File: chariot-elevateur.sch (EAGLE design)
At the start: 0 parts

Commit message: Placement des gros composants
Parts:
- added AX12_AR, AX12_AV: DYNAMIXEL-1X03AX, 1NTech_pinhead:DYNAMIXEL-1X03AX
- added ENCODEUR_DROIT, ENCODEUR_GAUCHE: JST-04GH-V, con-jst:JST-04GH-V
- added JUMPER: JST-03, con-jst:JST-03
- added LED2: green, led:LEDSMT1206
- added LED3: orange, led:LEDSMT1206
- added PAS_A_PAS: (no value), jst-ph:JST-PH6
- added Q1: BSS138, transistor-small-signal:BSS123
- added R2, R3: 10k, resistor:R-EU_R0805
- added R4, R5: 330, resistor:R-EU_R0805
- added S1: A4988-BREAKOUT, stepper:A4988-BREAKOUT
- added S3: TL36PO, switch:TL36PO
- added U$1: TEENSY_3.5_DIL+USB, Teensy_libSG:TEENSY_3.5_DIL+USB
- added U1: WIZ820IO, wiznet:WIZ820IO
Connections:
- new net +3V3: Q1.G, R2.1, R5.1, S3.S
- new net +5V: R3.1
- new net CHOOSE_COLOR: LED3.C, R4.2, S3.P
- new net GND: LED2.C, S3.O
- new net N$7: LED2.A, R4.1
- new net N$8: LED3.A, R5.2
- new net SERIAL_AX12: Q1.S, R2.2
- new net SERIAL_AX12_5V: Q1.D, R3.2

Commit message: more components
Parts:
- added ENDSTOP: JST-03, con-jst:JST-03
- added FUMIGENE: DYNAMIXEL-1X03XL, 1NTech_pinhead:DYNAMIXEL-1X03XL
- added PHARES_AR, PHARES_AV: JST-05, con-jst:JST-05
- added RASPBERRY: JST-06, con-jst:JST-06
- added TOF_AR: JST-08, con-jst:JST-08
- added VESC: (no value), pinhead:PINHD-1X3
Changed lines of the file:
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@@
 <part name="R3" library="resistor" library_urn="urn:adsk.eagle:library:348" deviceset="R-EU_" device="R0805" package3d_urn="urn:adsk.eagle:package:26059/1" value="10k"/>
 <part name="SUPPLY26" library="supply2" library_urn="urn:adsk.eagle:library:372" deviceset="+5V" device=""/>
+<part name="VESC" library="pinhead" library_urn="urn:adsk.eagle:library:325" deviceset="PINHD-1X3" device="" package3d_urn="urn:adsk.eagle:package:22458/2"/>
+<part name="TOF_AR" library="con-jst" deviceset="JST-08" device=""/>
+<part name="PHARES_AR" library="con-jst" deviceset="JST-05" device=""/>
+<part name="PHARES_AV" library="con-jst" deviceset="JST-05" device=""/>
+<part name="FUMIGENE" library="1NTech_pinhead" deviceset="DYNAMIXEL-1X03" device="XL"/>
+<part name="ENDSTOP" library="con-jst" deviceset="JST-03" device=""/>
+<part name="RASPBERRY" library="con-jst" deviceset="JST-06" device=""/>
 </parts>
 <sheets>
@@
 <attribute name="VALUE" x="48.895" y="86.995" size="1.778" layer="96"/>
 </instance>
+<instance part="VESC" gate="A" x="35.56" y="116.84" smashed="yes">
+<attribute name="NAME" x="29.21" y="122.555" size="1.778" layer="95"/>
+<attribute name="VALUE" x="29.21" y="109.22" size="1.778" layer="96"/>
+</instance>
+<instance part="TOF_AR" gate="G$1" x="66.04" y="121.92" smashed="yes">
+<attribute name="NAME" x="62.992" y="124.714" size="1.778" layer="95"/>
+</instance>
+<instance part="PHARES_AR" gate="G$1" x="88.9" y="114.3" smashed="yes">
+<attribute name="NAME" x="85.852" y="117.094" size="1.778" layer="95"/>
+</instance>
+<instance part="PHARES_AV" gate="G$1" x="106.68" y="114.3" smashed="yes">
+<attribute name="NAME" x="103.632" y="117.094" size="1.778" layer="95"/>
+</instance>
+<instance part="FUMIGENE" gate="G$1" x="127" y="109.22" smashed="yes" rot="R90"/>
+<instance part="ENDSTOP" gate="G$1" x="33.02" y="106.68" smashed="yes">
+<attribute name="NAME" x="29.972" y="109.474" size="1.778" layer="95"/>
+</instance>
+<instance part="RASPBERRY" gate="G$1" x="88.9" y="93.98" smashed="yes">
+<attribute name="NAME" x="85.852" y="96.774" size="1.778" layer="95"/>
+</instance>
 </instances>

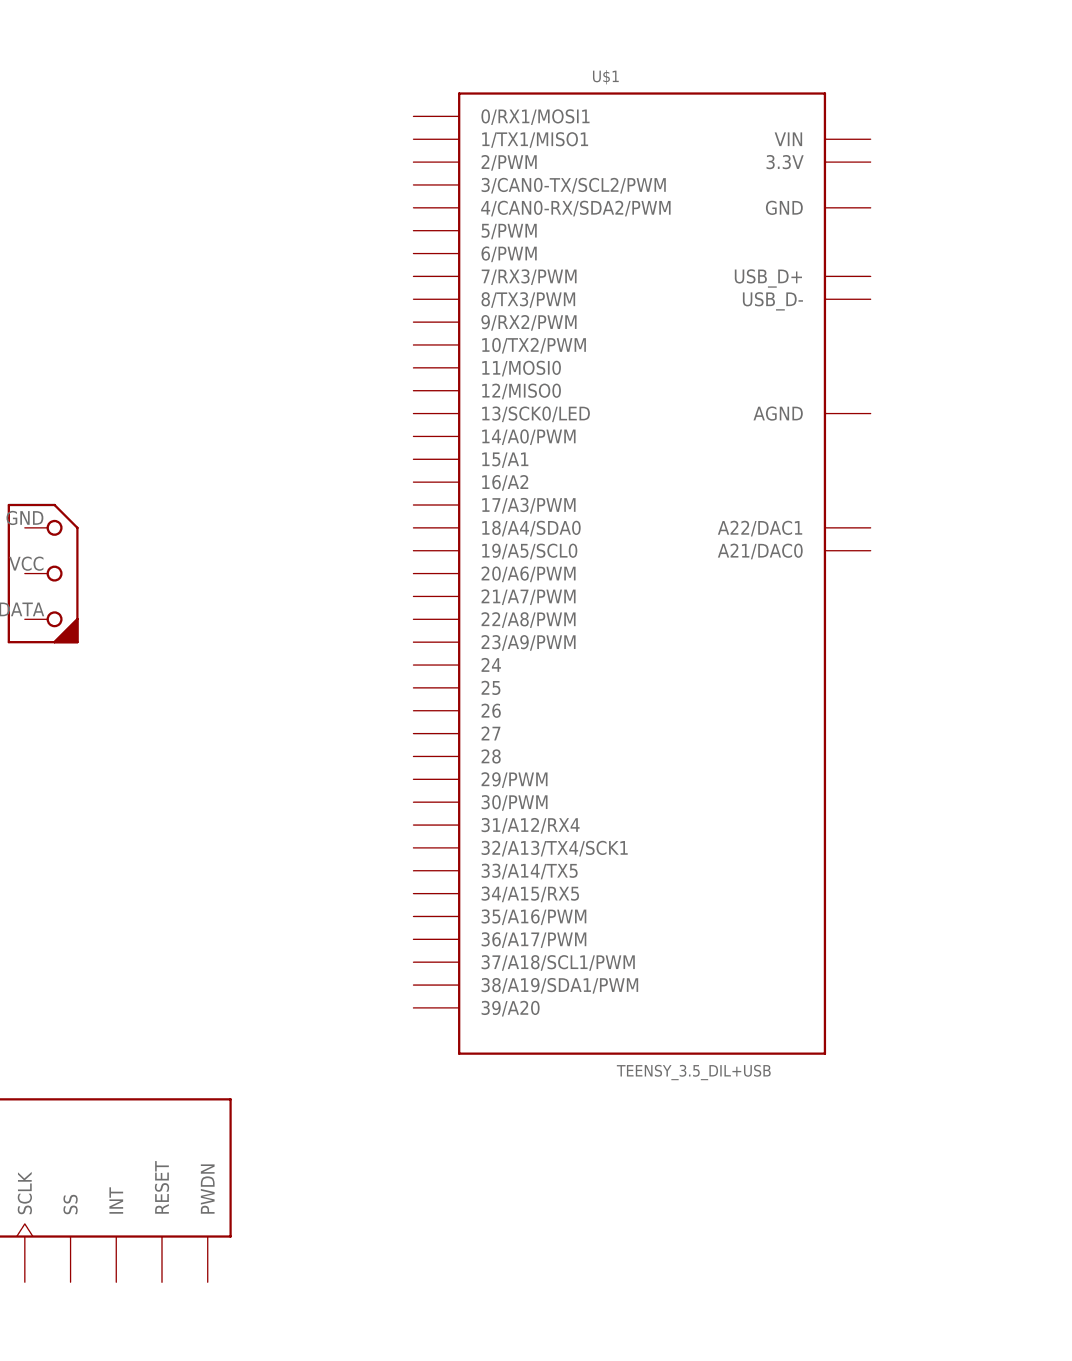
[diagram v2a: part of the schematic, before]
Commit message: Add power connector
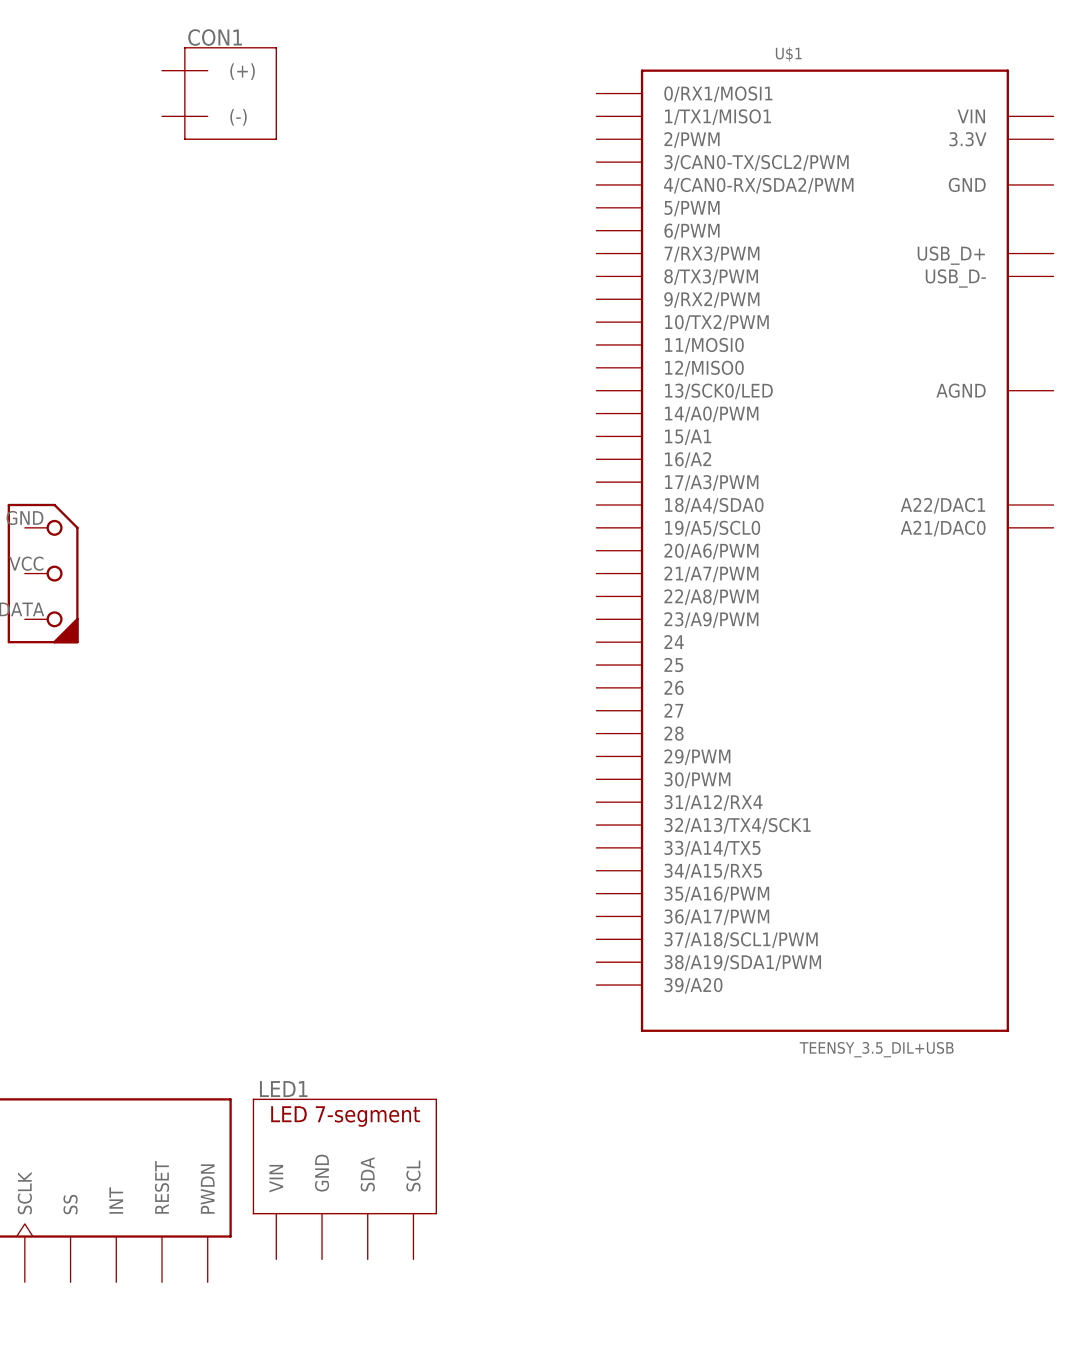
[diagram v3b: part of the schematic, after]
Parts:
- added CON1: XT-60, con-xt:XT-60
- added LED1: ADAFRUIT_7-SEGMENT-LED, Adafruit-7-segment:ADAFRUIT_7-SEGMENT-LED
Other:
- moved on the sheet: U$1
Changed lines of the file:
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@@
 <part name="ENDSTOP" library="con-jst" deviceset="JST-03" device=""/>
 <part name="RASPBERRY" library="con-jst" deviceset="JST-06" device=""/>
+<part name="LED1" library="Adafruit-7-segment" deviceset="ADAFRUIT_7-SEGMENT-LED" device=""/>
+<part name="CON1" library="con-xt" deviceset="XT-60" device=""/>
 </parts>
 <sheets>
@@
 <attribute name="SHEET" x="230.505" y="5.08" size="2.54" layer="94"/>
 </instance>
-<instance part="U$1" gate="G$1" x="195.58" y="109.22" smashed="yes">
-<attribute name="NAME" x="189.992" y="163.83" size="1.27" layer="95" font="vector" ratio="15"/>
-<attribute name="VALUE" x="192.786" y="53.34" size="1.27" layer="96" font="vector" ratio="15"/>
+<instance part="U$1" gate="G$1" x="215.9" y="111.76" smashed="yes">
+<attribute name="NAME" x="210.312" y="166.37" size="1.27" layer="95" font="vector" ratio="15"/>
+<attribute name="VALUE" x="213.106" y="55.88" size="1.27" layer="96" font="vector" ratio="15"/>
 </instance>
 <instance part="U1" gate="G$1" x="127" y="35.56" smashed="yes"/>
@@
 <attribute name="NAME" x="85.852" y="96.774" size="1.778" layer="95"/>
 </instance>
+<instance part="LED1" gate="G$1" x="162.56" y="38.1" smashed="yes">
+<attribute name="NAME" x="152.908" y="51.054" size="1.778" layer="95"/>
+</instance>
+<instance part="CON1" gate="G$1" x="147.32" y="162.56" smashed="yes">
+<attribute name="NAME" x="145.034" y="167.894" size="1.778" layer="95"/>
+</instance>
 </instances>

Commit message: placement connecteurs
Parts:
- VESC: device pinhead:PINHD-1X3 -> pinhead:PINHD-1X3/90
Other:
- moved on the sheet: CON1
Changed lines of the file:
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@@
 <part name="PAS_A_PAS" library="jst-ph" deviceset="JST-PH6" device=""/>
 <part name="S1" library="stepper" deviceset="A4988-BREAKOUT" device=""/>
-<part name="S3" library="switch" library_urn="urn:adsk.eagle:library:380" deviceset="TL36PO" device="" package3d_urn="urn:adsk.eagle:package:27745/1">
+<part name="S3" library="switch" deviceset="TL36PO" device="" package3d_urn="urn:adsk.eagle:package:27745/1">
 <attribute name="RS" value="913-9069"/>
 </part>
-<part name="LED2" library="led" library_urn="urn:adsk.eagle:library:259" deviceset="LED" device="SMT1206" package3d_urn="urn:adsk.eagle:package:15796/1" value="green"/>
-<part name="LED3" library="led" library_urn="urn:adsk.eagle:library:259" deviceset="LED" device="SMT1206" package3d_urn="urn:adsk.eagle:package:15796/1" value="orange"/>
+<part name="LED2" library="led" library_urn="urn:adsk.eagle:library:259" deviceset="LED" device="SMT1206" package3d_urn="urn:adsk.eagle:package:15796/2" value="green"/>
+<part name="LED3" library="led" library_urn="urn:adsk.eagle:library:259" deviceset="LED" device="SMT1206" package3d_urn="urn:adsk.eagle:package:15796/2" value="orange"/>
 <part name="SUPPLY27" library="supply2" library_urn="urn:adsk.eagle:library:372" deviceset="GND" device=""/>
-<part name="R4" library="resistor" library_urn="urn:adsk.eagle:library:348" deviceset="R-EU_" device="R0805" package3d_urn="urn:adsk.eagle:package:26059/1" value="330"/>
-<part name="R5" library="resistor" library_urn="urn:adsk.eagle:library:348" deviceset="R-EU_" device="R0805" package3d_urn="urn:adsk.eagle:package:26059/1" value="330"/>
-<part name="Q1" library="transistor-small-signal" library_urn="urn:adsk.eagle:library:401" deviceset="BSS123" device="" package3d_urn="urn:adsk.eagle:package:29752/1" value="BSS138"/>
-<part name="R2" library="resistor" library_urn="urn:adsk.eagle:library:348" deviceset="R-EU_" device="R0805" package3d_urn="urn:adsk.eagle:package:26059/1" value="10k"/>
-<part name="R3" library="resistor" library_urn="urn:adsk.eagle:library:348" deviceset="R-EU_" device="R0805" package3d_urn="urn:adsk.eagle:package:26059/1" value="10k"/>
+<part name="R4" library="resistor" library_urn="urn:adsk.eagle:library:348" deviceset="R-EU_" device="R0805" package3d_urn="urn:adsk.eagle:package:23553/2" value="330"/>
+<part name="R5" library="resistor" library_urn="urn:adsk.eagle:library:348" deviceset="R-EU_" device="R0805" package3d_urn="urn:adsk.eagle:package:23553/2" value="330"/>
+<part name="Q1" library="transistor-small-signal" library_urn="urn:adsk.eagle:library:401" deviceset="BSS123" device="" package3d_urn="urn:adsk.eagle:package:28738/2" value="BSS138"/>
+<part name="R2" library="resistor" library_urn="urn:adsk.eagle:library:348" deviceset="R-EU_" device="R0805" package3d_urn="urn:adsk.eagle:package:23553/2" value="10k"/>
+<part name="R3" library="resistor" library_urn="urn:adsk.eagle:library:348" deviceset="R-EU_" device="R0805" package3d_urn="urn:adsk.eagle:package:23553/2" value="10k"/>
 <part name="SUPPLY26" library="supply2" library_urn="urn:adsk.eagle:library:372" deviceset="+5V" device=""/>
-<part name="VESC" library="pinhead" library_urn="urn:adsk.eagle:library:325" deviceset="PINHD-1X3" device="" package3d_urn="urn:adsk.eagle:package:22458/2"/>
+<part name="VESC" library="pinhead" library_urn="urn:adsk.eagle:library:325" deviceset="PINHD-1X3" device="/90" package3d_urn="urn:adsk.eagle:package:22459/2"/>
 <part name="TOF_AR" library="con-jst" deviceset="JST-08" device=""/>
 <part name="PHARES_AR" library="con-jst" deviceset="JST-05" device=""/>
@@
 <attribute name="NAME" x="152.908" y="51.054" size="1.778" layer="95"/>
 </instance>
-<instance part="CON1" gate="G$1" x="147.32" y="162.56" smashed="yes">
-<attribute name="NAME" x="145.034" y="167.894" size="1.778" layer="95"/>
+<instance part="CON1" gate="G$1" x="144.78" y="160.02" smashed="yes">
+<attribute name="NAME" x="142.494" y="165.354" size="1.778" layer="95"/>
 </instance>
 </instances>

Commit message: end-of-the-day commit
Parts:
- removed RASPBERRY: JST-06, con-jst:JST-06
- added C1, C2, C3, C4: 22µF, resistor:C-EUC0805
- added C5, C6: 1µF, resistor:C-EUC0805
- added D1: DIODE_S15P45, diode_schottky:DIODE_S15P45
- added DC1, DC2: TSR 1-2450, dc-dc-converter:R-78C5.0-1.0
- added DC3: TSR 2-2450, dc-dc-converter:R-78C5.0-1.0
- added DC4: TSR 2-24120, dc-dc-converter:R-78C12-1.0
- added P1: RG500, polyswitch:RGEF800
- added R1: 10k, resistor:R-EU_R0805
- added SJ1: (no value), jumper:SJ2W
- added TOF_AV: JST-08, con-jst:JST-08
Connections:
- removed net +5V: R3.1
- new net +12V: AX12_AR.DYN_VCC, AX12_AV.DYN_VCC, C5.2, C6.2, SJ1.2
- new net +24V: C1.1, C2.1, C3.1, C4.1, D1.-, DC1.VIN, DC2.VIN, DC3.VIN, DC4.VIN, S1.VMOT, SJ1.1
- new net +5V/1: DC1.VOUT, ENCODEUR_DROIT.1, ENCODEUR_GAUCHE.1, R3.1, U$1.VIN
- new net +5V/2: DC2.VOUT, PHARES_AR.3, PHARES_AR.4, PHARES_AV.3, PHARES_AV.4
- new net +5V/3: DC3.VOUT
- new net DEL_AR: PHARES_AR.5
- new net DEL_AV: PHARES_AV.5
- new net DIR: S1.DIR, U$1.3/CAN0-TX/SCL2/PWM
- new net ENC_D_A: ENCODEUR_DROIT.3
- new net ENC_D_B: ENCODEUR_DROIT.4
- new net ENC_G_A: ENCODEUR_GAUCHE.3
- new net ENC_G_B: ENCODEUR_GAUCHE.4
- new net ENDSTOP: ENDSTOP.3
- new net ETH_MISO: U$1.12/MISO0, U1.MISO
- new net ETH_MOSI: U$1.11/MOSI0, U1.MOSI
- new net ETH_RST: R1.1, U$1.15/A1, U1.RESET
- new net ETH_SCLK: U$1.13/SCK0/LED, U1.SCLK
- new net ETH_SS: U$1.10/TX2/PWM, U1.SS
- new net FUM_POMPE: FUMIGENE.DYN_VCC
- new net FUM_RES: FUMIGENE.DATA
- new net JUMPER: JUMPER.3
- new net N$1: CON1.(+), P1.2
- new net N$10: U$1.25
- new net N$11: U$1.26
- new net N$12: U$1.27
- new net N$13: U$1.28
- new net N$14: U$1.29/PWM
- new net N$15: U$1.30/PWM
- new net N$16: U$1.31/A12/RX4
- new net N$17: U$1.32/A13/TX4/SCK1
- new net N$18: U$1.33/A14/TX5
- new net N$19: U$1.34/A15/RX5
- new net N$2: PAS_A_PAS.2, S1.1B
- new net N$20: U$1.35/A16/PWM
- new net N$21: U$1.36/A17/PWM
- new net N$22: U$1.5/PWM
- new net N$23: U$1.6/PWM
- new net N$24: U$1.24
- new net N$25: U$1.37/A18/SCL1/PWM
- new net N$26: U$1.38/A19/SDA1/PWM
- new net N$3: PAS_A_PAS.3, S1.1A
- new net N$4: D1.+, P1.1
- new net N$5: PAS_A_PAS.4, S1.2A
- new net N$6: PAS_A_PAS.5, S1.2B
- new net N$9: DC4.VOUT, SJ1.3
- new net SCL: LED1.SCL, TOF_AR.4, TOF_AV.4, U$1.19/A5/SCL0
- new net SDA: LED1.SDA, TOF_AR.3, TOF_AV.3, U$1.18/A4/SDA0
- new net STEP: S1.STEP, U$1.4/CAN0-RX/SDA2/PWM
- new net TOF_AR_D: TOF_AR.7
- new net TOF_AR_FD: TOF_AR.8
- new net TOF_AR_FG: TOF_AR.5
- new net TOF_AR_G: TOF_AR.6
- new net TOF_AV_D: TOF_AV.8
- new net TOF_AV_G: TOF_AV.5
- new net TOF_AV_SD: TOF_AV.7
- new net TOF_AV_SG: TOF_AV.6
- new net VESC_CMD: U$1.2/PWM, VESC.1
- net +3V3: now also ENDSTOP.2, JUMPER.2, LED1.VIN, S1.VDD, TOF_AR.2, TOF_AV.2, U$1.3.3V, U1.VIN3V3
- net CHOOSE_COLOR: now also U$1.39/A20
- net GND: now also AX12_AR.GND, AX12_AV.GND, C1.2, C2.2, C3.2, C4.2, C5.1, C6.1, CON1.(-), DC1.GND, DC2.GND, DC3.GND, DC4.GND, ENCODEUR_DROIT.2, ENCODEUR_GAUCHE.2, ENDSTOP.1, FUMIGENE.GND, JUMPER.1, LED1.GND, PHARES_AR.1, PHARES_AR.2, PHARES_AV.1, PHARES_AV.2, R1.2, S1.GND, TOF_AR.1, TOF_AV.1, U$1.AGND, U$1.GND, U1.GND, U1.PWDN, VESC.3
- net SERIAL_AX12: now also U$1.0/RX1/MOSI1, U$1.1/TX1/MISO1
- net SERIAL_AX12_5V: now also AX12_AR.DATA, AX12_AV.DATA
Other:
- moved on the sheet: CON1, ENCODEUR_DROIT, ENCODEUR_GAUCHE, ENDSTOP, JUMPER, LED1, LED2, LED3, PAS_A_PAS, PHARES_AR, PHARES_AV, Q1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

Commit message: end-of-day commit
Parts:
- renumbered U$1 to TEENSY
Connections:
- removed net N$10: TEENSY.25
- removed net N$13: TEENSY.28
- removed net N$14: TEENSY.29/PWM
- removed net N$15: TEENSY.30/PWM
- removed net N$16: TEENSY.31/A12/RX4
- removed net N$18: TEENSY.33/A14/TX5
- removed net N$19: TEENSY.34/A15/RX5
- removed net N$20: TEENSY.35/A16/PWM
- removed net N$21: TEENSY.36/A17/PWM
- removed net N$23: TEENSY.6/PWM
- removed net N$24: TEENSY.24
- removed net N$25: TEENSY.37/A18/SCL1/PWM
- removed net N$26: TEENSY.38/A19/SDA1/PWM
- new net FUM_POMPE_CMD: TEENSY.20/A6/PWM
- new net FUM_RES_CMD: TEENSY.14/A0/PWM
- new net S_MS1: S1.MS1, TEENSY.28
- new net S_MS2: S1.MS2, TEENSY.27
- new net S_MS3: S1.MS3, TEENSY.26
- new net S_N_RST: S1.N_RESET, TEENSY.32/A13/TX4/SCK1
- new net S_N_SLEEP: S1.N_SLEEP, TEENSY.31/A12/RX4
- net CHOOSE_COLOR: now also TEENSY.8/TX3/PWM; no longer TEENSY.39/A20
- net DEL_AR: now also TEENSY.6/PWM
- net DEL_AV: now also TEENSY.7/RX3/PWM
- net DIR: now also TEENSY.29/PWM; no longer TEENSY.3/CAN0-TX/SCL2/PWM
- net ENC_D_A: now also TEENSY.39/A20
- net ENC_D_B: now also TEENSY.38/A19/SDA1/PWM
- net ENC_G_A: now also TEENSY.34/A15/RX5
- net ENC_G_B: now also TEENSY.33/A14/TX5
- net ENDSTOP: now also TEENSY.9/RX2/PWM
- net JUMPER: now also TEENSY.37/A18/SCL1/PWM
- net N$11: now also TEENSY.4/CAN0-RX/SDA2/PWM; no longer TEENSY.26
- net N$12: now also TEENSY.3/CAN0-TX/SCL2/PWM; no longer TEENSY.27
- net N$17: now also TEENSY.2/PWM; no longer TEENSY.32/A13/TX4/SCK1
- net STEP: now also TEENSY.30/PWM; no longer TEENSY.4/CAN0-RX/SDA2/PWM
- net TOF_AR_D: now also TEENSY.23/A9/PWM
- net TOF_AR_FD: now also TEENSY.16/A2
- net TOF_AR_FG: now also TEENSY.21/A7/PWM
- net TOF_AR_G: now also TEENSY.22/A8/PWM
- net TOF_AV_D: now also TEENSY.35/A16/PWM
- net TOF_AV_G: now also TEENSY.24
- net TOF_AV_SD: now also TEENSY.36/A17/PWM
- net TOF_AV_SG: now also TEENSY.25
- net VESC_CMD: now also TEENSY.17/A3/PWM; no longer TEENSY.2/PWM

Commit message: v1
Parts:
- removed C5, C6: 1µF, resistor:C-EUC0805
- added C10, C11, C12, C13: 10µF/50V, resistor:C-EUC1210
- added C14, C15: 1µF, resistor:C-EUC0805
- added C7, C9: 220µF/25V, resistor:CPOL-EUE3.5-8
- added C8: 100µF/50V, resistor:CPOL-EUE3.5-8
- added Q2: DMN2056U, transistor-small-signal:BSS123
- added R6: 10k, resistor:R-EU_R0805
- added R7: 100, resistor:R-EU_R0805
- added USB: (no value), pinhead:PINHD-1X3
- C1, C2, C3, C4: value 22µF -> 10µF/50V; device resistor:C-EUC0805 -> resistor:C-EUC1210
- Q1: value BSS138 -> DMN2056U; RS (none) -> 133-3376
- R3: value 10k -> 100
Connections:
- net N$1 renamed V_LIPO
- removed net DEL_AR: PHARES_AR.5, TEENSY.6/PWM
- removed net DEL_AV: PHARES_AV.5, TEENSY.7/RX3/PWM
- removed net FUM_POMPE_CMD: TEENSY.20/A6/PWM
- removed net FUM_RES_CMD: TEENSY.14/A0/PWM
- removed net N$11: TEENSY.4/CAN0-RX/SDA2/PWM
- removed net N$12: TEENSY.3/CAN0-TX/SCL2/PWM
- removed net N$17: TEENSY.2/PWM
- removed net N$22: TEENSY.5/PWM
- new net CMD_DEL_AR: TEENSY.6/PWM
- new net CMD_DEL_AR_5V: PHARES_AR.5
- new net CMD_DEL_AV: TEENSY.7/RX3/PWM
- new net CMD_DEL_AV_5V: PHARES_AV.5
- new net CMD_FUM_POMPE: R3.1, TEENSY.20/A6/PWM
- new net CMD_FUM_RES: R7.1, TEENSY.14/A0/PWM
- new net HV: R2.1
- new net IO_HV: Q1.D, R2.2
- new net IO_LV: Q1.S, R1.2
- new net LV: Q1.G, R1.1
- new net N$10: Q1.G, R2.1, R3.2
- new net N$13: Q2.G, R6.1, R7.2
- new net SCL_5V: LED1.SCL
- new net SDA_5V: LED1.SDA
- new net USB_D+: TEENSY.USB_D+, USB.1
- new net USB_D-: TEENSY.USB_D-, USB.2
- net +12V: now also C14.2, C15.2; no longer C5.2, C6.2
- net +24V: now also C10.1, C11.1, C12.1, C13.1, C8.+
- net +3V3: no longer LED1.VIN, Q1.G, R2.1
- net +5V/1: now also LED1.VIN; no longer R3.1
- net +5V/2: now also C7.+
- net +5V/3: now also C9.+, FUMIGENE.DYN_VCC
- net FUM_POMPE: now also FUMIGENE.GND, Q1.D; no longer FUMIGENE.DYN_VCC
- net FUM_RES: now also Q2.D
- net GND: now also C10.2, C11.2, C12.2, C13.2, C14.1, C15.1, C7.-, C8.-, C9.-, Q1.S, Q2.S, R2.2, R6.2, USB.3; no longer C5.1, C6.1, FUMIGENE.GND
- net SCL: no longer LED1.SCL
- net SDA: no longer LED1.SDA
- net SERIAL_AX12: no longer Q1.S, R2.2
- net SERIAL_AX12_5V: no longer Q1.D, R3.2
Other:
- moved on the sheet: C1, C2, C3, C4, DC1, DC2, DC3, DC4, PAS_A_PAS, Q1, R2, R3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
